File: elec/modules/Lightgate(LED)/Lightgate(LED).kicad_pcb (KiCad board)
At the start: 2 copper layers, 24.4 x 47.7 mm, 2 parts, among them J1 Conn_01x02

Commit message: idk
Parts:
- J1: footprint Pinheaders:PinHeader_1x02_P2.54mm_Vertical -> Connector_JST:JST_SH_BM02B-SRSS-TB_1x02-1MP_P1.00mm_Vertical
- moved J1 45.5 mm to (92.5, 77.2)
- moved LED7 41.4 mm to (105.4, 66.2), turned to 90 degrees

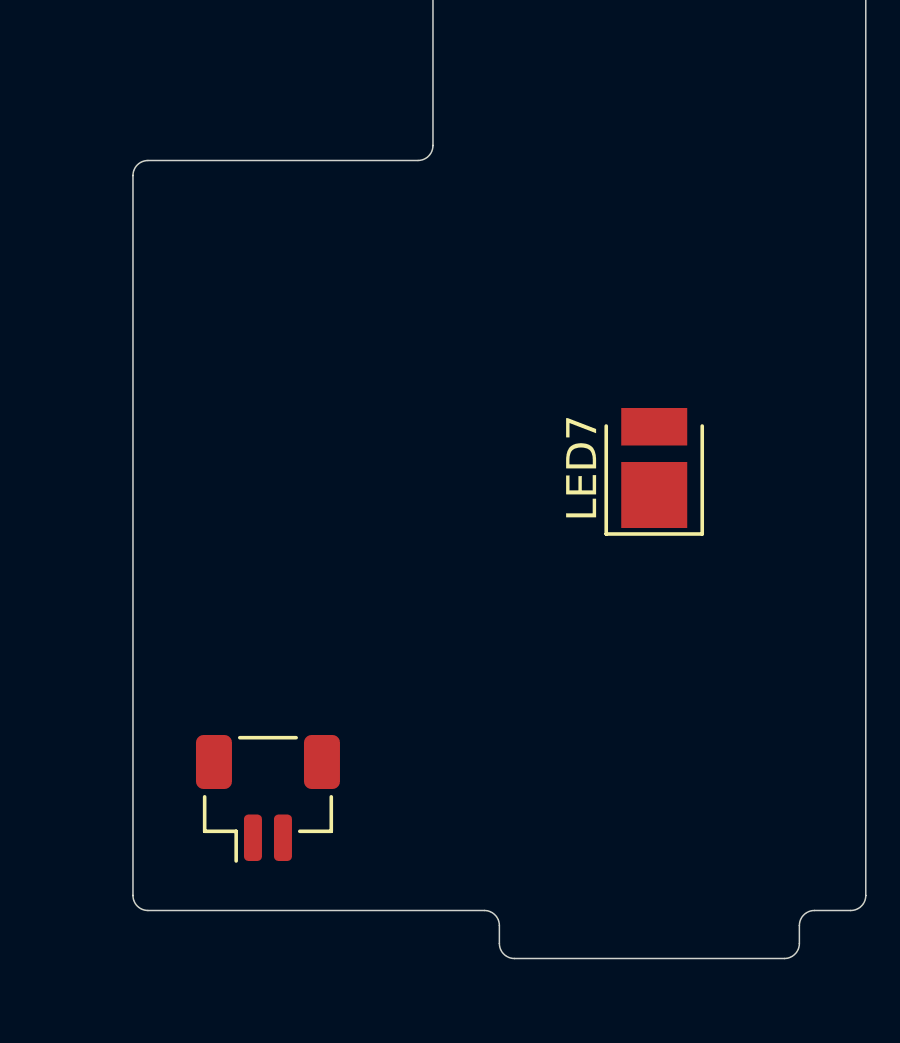
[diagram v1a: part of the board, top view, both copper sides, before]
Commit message: fixed light gate jst
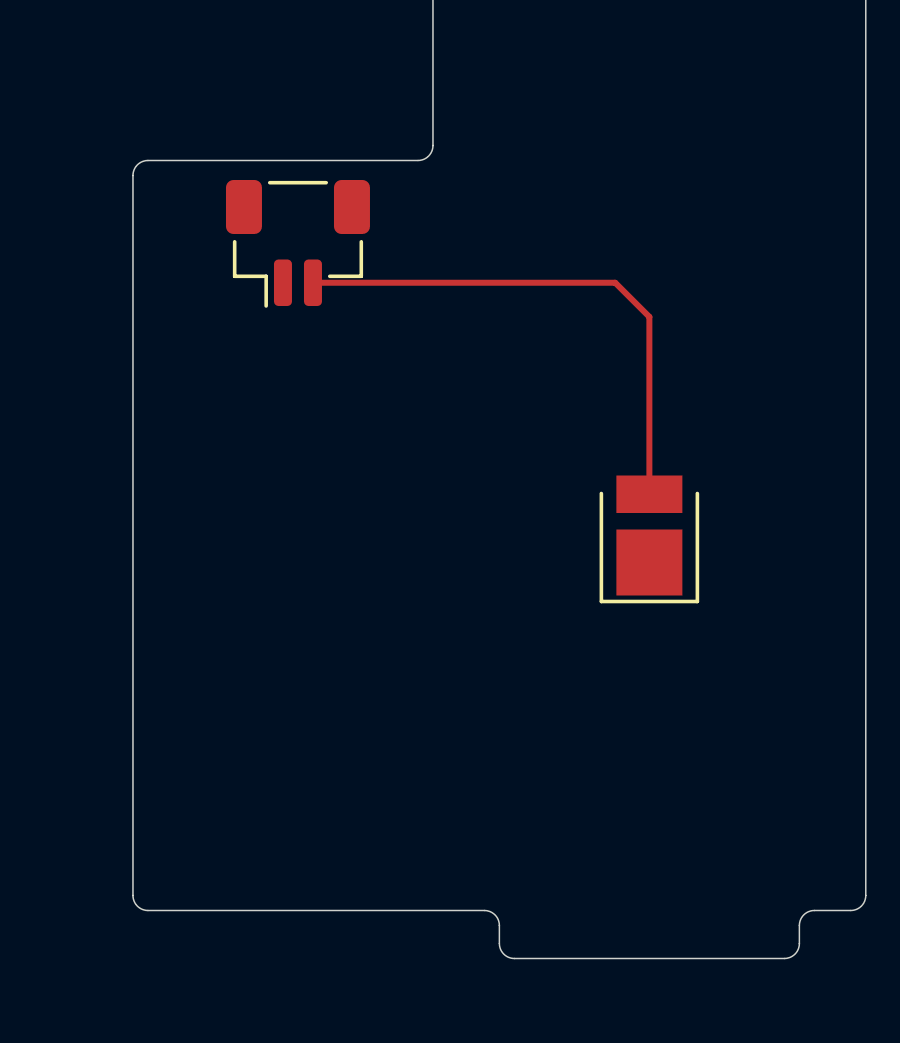
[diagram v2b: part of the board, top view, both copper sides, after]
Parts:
- moved J1 18.5 mm to (93.5, 58.8)
- moved LED7 2.26 mm to (105.2, 68.5)
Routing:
- net +3V3: track 0.00 -> 17.6 mm
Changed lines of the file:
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@@
 	(footprint "Connector_JST:JST_SH_BM02B-SRSS-TB_1x02-1MP_P1.00mm_Vertical"
 		(layer "F.Cu")
-		(at 92.5 77.25)
+		(at 93.5 58.75)
 		(descr "JST SH series connector, BM02B-SRSS-TB (http://www.jst-mfg.com/product/pdf/eng/eSH.pdf), generated with kicad-footprint-generator")
 		(tags "connector JST SH vertical")
@@
 		)
 		(embedded_fonts no)
-		(model "${KICAD9_3DMODEL_DIR}/Connector_JST.3dshapes/JST_SH_BM02B-SRSS-TB_1x02-1MP_P1.00mm_Vertical.step"
+		(model "C:/Users/Eusto/Documents/Cup/robocup2026-i2/elec/modules/references/LightGatejst 3d model/S2B-PH-SM4-TB--3DModel-STEP-269445.STEP"
 			(offset
-				(xyz 0 0 0)
+				(xyz 0 4 0)
 			)
 			(scale
@@
 			)
 			(rotate
-				(xyz 0 0 0)
+				(xyz 90 -180 -0)
 			)
 		)
@@
 	(footprint "LED_SMD:LED_PLCC_2835"
 		(layer "F.Cu")
-		(at 105.375 66.25 90)
+		(at 105.213458 68.499999 90)
 		(descr "https://www.luckylight.cn/media/component/data-sheet/R2835BC-B2M-M10.pdf")
 		(tags "LED")
@@
 			(at 0 -2.4 90)
 			(layer "F.SilkS")
+			(hide yes)
 			(effects
 				(font
@@
 			(at 0 2.475 90)
 			(layer "F.Fab")
+			(hide yes)
 			(effects
 				(font
@@
 			)
 			(layer "F.Fab")
-		)
-		(fp_text user "${REFERENCE}"
-			(at 0 0 90)
-			(layer "F.Fab")
-			(effects
-				(font
-					(size 0.9 0.9)
-					(thickness 0.135)
-				)
-			)
 		)
 		(pad "1" smd rect
@@
 		(layer "Edge.Cuts")
 	)
+	(segment
+		(start 94 60.075)
+		(end 104.075 60.075)
+		(width 0.2)
+		(layer "F.Cu")
+		(net 1)
+	)
+	(segment
+		(start 104.075 60.075)
+		(end 105.213458 61.213458)
+		(width 0.2)
+		(layer "F.Cu")
+		(net 1)
+	)
+	(segment
+		(start 105.213458 61.213458)
+		(end 105.213458 67.124999)
+		(width 0.2)
+		(layer "F.Cu")
+		(net 1)
+	)
 	(zone
 		(net 2)
@@
 		(layers "F.Cu" "B.Cu")
 		(hatch edge 0.5)
-		(connect_pads
+		(connect_pads yes
 			(clearance 0.5)
 		)
@@
 			(thermal_gap 0.5)
 			(thermal_bridge_width 0.5)
+			(smoothing chamfer)
+			(radius 0.25)
 		)
 		(polygon
